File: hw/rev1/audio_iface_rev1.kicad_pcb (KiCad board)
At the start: 2 copper layers, 122 parts, among them J101 CONN_2, J102 CONN_2, J103 CONN_2, J104 CONN_2, J105 CONN_2, J501 CONN_6, J601 CONN_2, Q201 BC550, Q202 BC550, U101 USBMICROCONN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

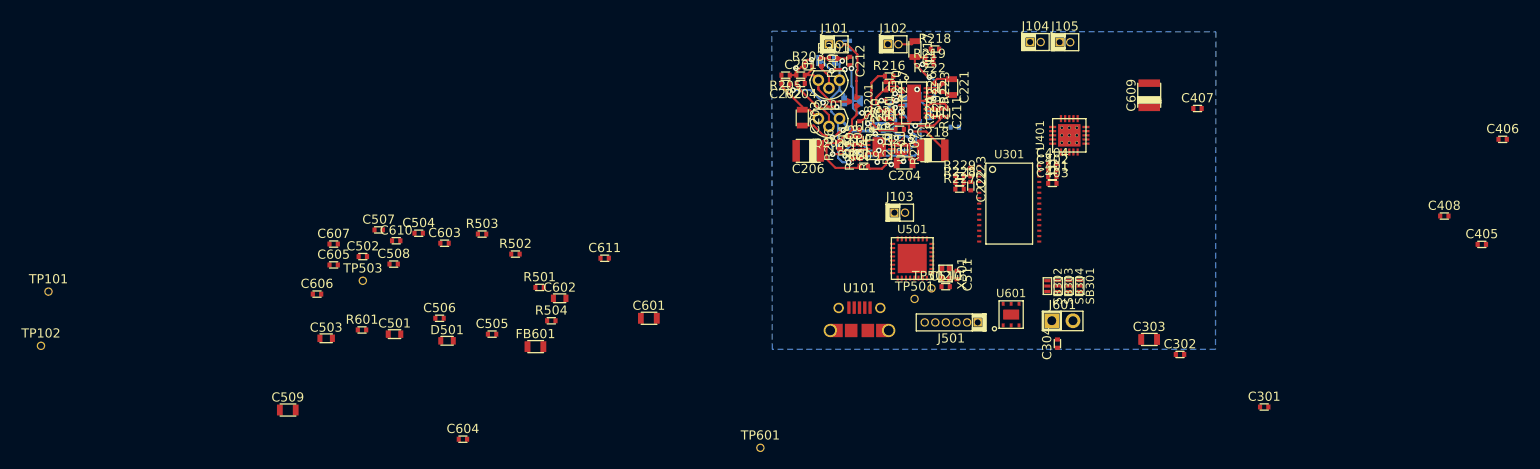
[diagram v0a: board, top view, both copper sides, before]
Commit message: Completed PCB with new K20x72 instead.
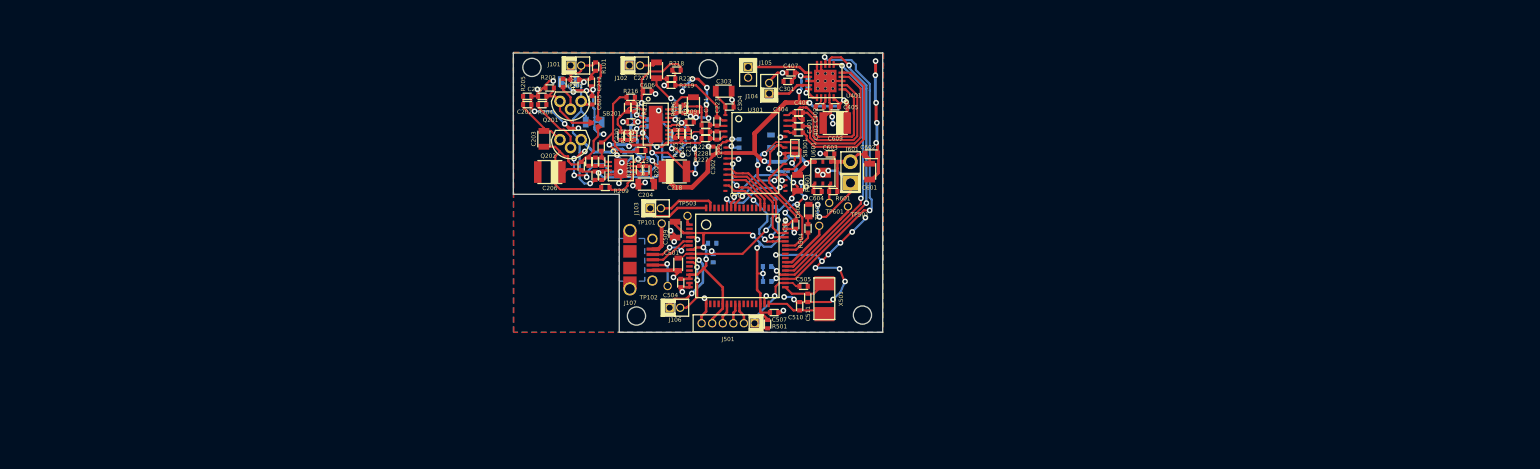
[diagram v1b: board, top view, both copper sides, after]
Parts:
- removed SB302, SB303, SB304: SB_2-1, SB_2-1
- added G***: LOGO, LOGO, F.Cu at (161.8, 112.7)
- added J106: CONN_2, HDR_2X1_50MIL, F.Cu at (140.6, 117.8)
- added SCREW_HOLE_2-56: VAL**, SCREW_HOLE_2-56, F.Cu at (163.1, 118.7)
- added SCREW_HOLE_2-56: VAL**, SCREW_HOLE_2-56, F.Cu at (144.6, 89.1)
- added SCREW_HOLE_2-56: VAL**, SCREW_HOLE_2-56, F.Cu at (123.5, 89.0)
- added SCREW_HOLE_2-56: VAL**, SCREW_HOLE_2-56, F.Cu at (136.0, 118.8)
- added VAL: OSHW, OSHW, B.Cu at (161.2, 113.3)
- C209, R101: moved to F.Cu
- C301: value 10u -> 1u
- C408, C502, C503, C508, C607, C610, C611, R502, R503: moved to B.Cu
- TP501: value TP_PTA1 -> TP_PTB3
- TP502: value TP_PTA4 -> TP_PTB16
- TP503: value TP_PTD5 -> TP_PTE0
- U501: value MK20DX128VFM5 -> K20X7_QFP64; footprint FREESCALE_QFN32 -> FREESCALE_QFP64
- X501: footprint XRCGB_F_N -> TXC_7A
- moved C406 82.0 mm to (158.0, 93.7), turned to 180 degrees
- moved C405 79.3 mm to (159.8, 93.7)
- moved C408 78.0 mm to (156.6, 90.8), turned to 270 degrees
- moved TP102 75.5 mm to (139.8, 115.2)
- moved TP101 74.0 mm to (139.0, 107.7)
- moved C301 69.2 mm to (154.2, 90.7)
- moved C302 61.1 mm to (145.2, 99.0), turned to 270 degrees
- moved C303 59.1 mm to (146.5, 91.8), turned to 180 degrees
- moved R601 58.9 mm to (159.6, 103.9), turned to 180 degrees
- moved C503 58.3 mm to (152.1, 97.8), turned to 270 degrees
- moved C604 51.9 mm to (157.7, 103.9), turned to 180 degrees
- moved C509 51.2 mm to (140.6, 108.4), turned to 90 degrees
- moved C607 50.1 mm to (148.3, 98.1), turned to 270 degrees
- moved C407 49.0 mm to (154.5, 89.6)
- moved C304 48.5 mm to (147.2, 93.7), turned to 180 degrees
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- renumbered U101 to J107
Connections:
- C301 pad 1: AGND_OUT -> AGND_IN
- C302 pad 1: AGND_OUT -> AGND_IN
- C303 pad 1: AGND_OUT -> AGND_IN
- C304 pad 1: AGND_OUT -> AGND_IN
- C401 pad 2: N-0000070 -> N-0000071
- C402 pad 2: N-0000066 -> N-0000070
- C403 pad 2: N-0000069 -> N-0000066
- C404 pad 2: N-0000068 (its old number) -> N-0000069
- C405 pad 1: AGND_OUT -> AGND_IN
- C407 pad 1: AGND_OUT -> AGND_IN
- C510 pad 1: N-0000084 -> N-00000103
- C511 pad 1: N-0000083 -> N-00000104
- J104 pad 2: AGND_OUT -> AGND_IN
- J105 pad 2: AGND_OUT -> AGND_IN
- J501 pad 1: /Microcontroller/SWCLK -> /Microcontroller/RESET
- J501 pad 3: /Microcontroller/RESET -> /Microcontroller/SWO
- J501 pad 4: /Microcontroller/SWO -> /Microcontroller/SWCLK
- R101 pad 2: +5V -> +5VA
- R218 pad 2: +5V -> +5VA
- R504 pad 2: N-0000074 -> N-0000091
- SB301 pad 1: N-0000060 -> N-0000063
- TP501 pad 1: N-0000075 -> N-0000090
- TP502 pad 1: N-0000072 (its old number) -> N-0000092
- TP503 pad 1: N-0000076 -> N-0000089
- U301 pad 17: N-0000060 -> /Microcontroller/SPI1_SOUT
- U301 pad 18: N-0000057 -> /Microcontroller/SPI1_SCK
- U301 pad 19: N-0000058 (its old number) -> /Microcontroller/SPI1_CS_CODEC
- U301 pad 22: +3V -> AGND_IN
- U301 pad 23: +3V -> AGND_IN
- U301 pad 7: AGND_OUT -> AGND_IN
- U301 pad 9: +5V -> AGND_IN
- U401 pad 1: N-0000069 -> N-0000070
- U401 pad 10: AGND_OUT -> AGND_IN
- U401 pad 13: AGND_OUT -> AGND_IN
- U401 pad 19: AGND_OUT -> AGND_IN
- U401 pad 2: N-0000070 -> N-0000069
- U401 pad 3: AGND_OUT -> AGND_IN
- U401 pad 4: N-0000068 (its old number) -> N-0000071
- U401 pad 9: AGND_OUT -> AGND_IN
- U401 pad PAD: AGND_OUT -> AGND_IN
- U501 pad 1: +3V -> N-0000089
- U501 pad 10: (no net) -> /Microcontroller/PGA0_D-
- U501 pad 11: +3V -> (no net)
- U501 pad 12: /Microcontroller/SWCLK -> (no net)
- U501 pad 13: N-0000075 -> +3V
- U501 pad 14: /Microcontroller/SWO -> +3V
- U501 pad 15: /Microcontroller/SWDIO -> AGND_IN
- U501 pad 16: N-0000072 (its old number) -> AGND_IN
- U501 pad 17: N-0000084 -> AGND_IN
- U501 pad 18: N-0000083 -> (no net)
- U501 pad 19: /Microcontroller/RESET -> (no net)
- U501 pad 2: AGND_IN -> (no net)
- U501 pad 20: /Microcontroller/I2C0_SCL -> (no net)
- U501 pad 21: /Microcontroller/I2C0_SDA -> +3V
- U501 pad 22: /Microcontroller/CODEC_SDO -> /Microcontroller/SWCLK
- U501 pad 23: /Microcontroller/CODEC_LRCK -> (no net)
- U501 pad 24: /CODEC/BICK -> /Microcontroller/SWO
- U501 pad 25: /Microcontroller/HP_~SD -> /Microcontroller/SWDIO
- U501 pad 26: /Microcontroller/CODEC_SDIN -> (no net)
- U501 pad 27: /Microcontroller/CODEC_MCLK -> (no net)
- U501 pad 28: N-0000074 -> (no net)
- U501 pad 29: /Microcontroller/CODEC_PDN -> (no net)
- U501 pad 3: /Microcontroller/USB_D+ -> +3V
- U501 pad 30: N-0000076 -> +3V
- U501 pad 31: /Microcontroller/UART0_RX -> AGND_IN
- U501 pad 32: /Microcontroller/UART0_TX -> N-00000103
- U501 pad 4: /Microcontroller/USB_D- -> AGND_IN
- U501 pad 5: +3V -> /Microcontroller/USB_D+
- U501 pad 6: +5V -> /Microcontroller/USB_D-
- U501 pad 8: AGND_IN -> +5V
- U501 pad 9: (no net) -> /Microcontroller/PGA0_D+
- X501 pad 1: N-0000083 -> N-00000104
- X501 pad 2: N-0000084 -> N-00000103
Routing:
- net AGND_IN: track 75.7 -> 209.8 mm, vias 25 -> 85
- net +5VA: track 41.2 -> 114.3 mm, vias 5 -> 13
- net +3V: track 0.00 -> 68.5 mm, vias 0 -> 8
- net /Microcontroller/I2C0_SCL: track 0.00 -> 38.8 mm, vias 0 -> 3
- net /Microcontroller/I2C0_SDA: track 0.00 -> 36.2 mm, vias 0 -> 3
- net /Microcontroller/HP_~SD: track 0.00 -> 31.2 mm, vias 0 -> 2
- net +5V: track 0.00 -> 29.6 mm, vias 0 -> 5
- net N-0000066: track 0.00 -> 18.3 mm
- net N-0000071: track 0.00 -> 17.8 mm
- net N-0000070: track 0.00 -> 17.7 mm
- net N-0000069: track 0.00 -> 16.7 mm
- net /Microcontroller/CODEC_LRCK: track 0.00 -> 14.1 mm, vias 0 -> 2
- net /Microcontroller/CODEC_PDN: track 0.00 -> 13.9 mm
- net /Microcontroller/CODEC_SDO: track 0.00 -> 12.8 mm, vias 0 -> 2
- net /CODEC/BICK: track 0.00 -> 11.9 mm
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- added copper zone on B.Cu, net (none)
- added copper zone on F.Cu, net AGND_IN
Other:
- board outline added: 44.3 x 33.5 mm
- board text added: "BRN"
- board text added: "EXT"
- board text added: "MIC"
- board text added: "R"
- board text added: "T"
- board text added: "r1a"

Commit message: Added supply voltage ADC input to monitor battery levels
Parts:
- added C512: 1u, SMD0402, B.Cu at (162.1, 105.8)
- added R505: 330k, SMD0402, B.Cu at (160.4, 105.8)
- added R506: 100k, SMD0402, B.Cu at (161.3, 105.8)
- moved TP501 4.29 mm to (157.8, 108.0)
- moved TP502 1.52 mm to (159.0, 106.9)
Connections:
- TP501 pad 1: N-0000090 -> N-0000089
- U501 pad 38: N-0000090 -> N-00000101
- U501 pad 40: (no net) -> N-0000089
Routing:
- net N-00000101: track 0.00 -> 11.4 mm, vias 0 -> 1
- net N-0000090: track 10.9 -> 0.00 mm
- net N-0000089: track 0.00 -> 5.83 mm
- net AGND_IN: track 209.8 -> 204.2 mm, vias 85 -> 83
- net VCC: track 10.8 -> 12.4 mm, vias 0 -> 1
- net (no net): track 0.00 -> 1.56 mm, vias 0 -> 2
- net N-0000080: track 6.52 -> 8.08 mm

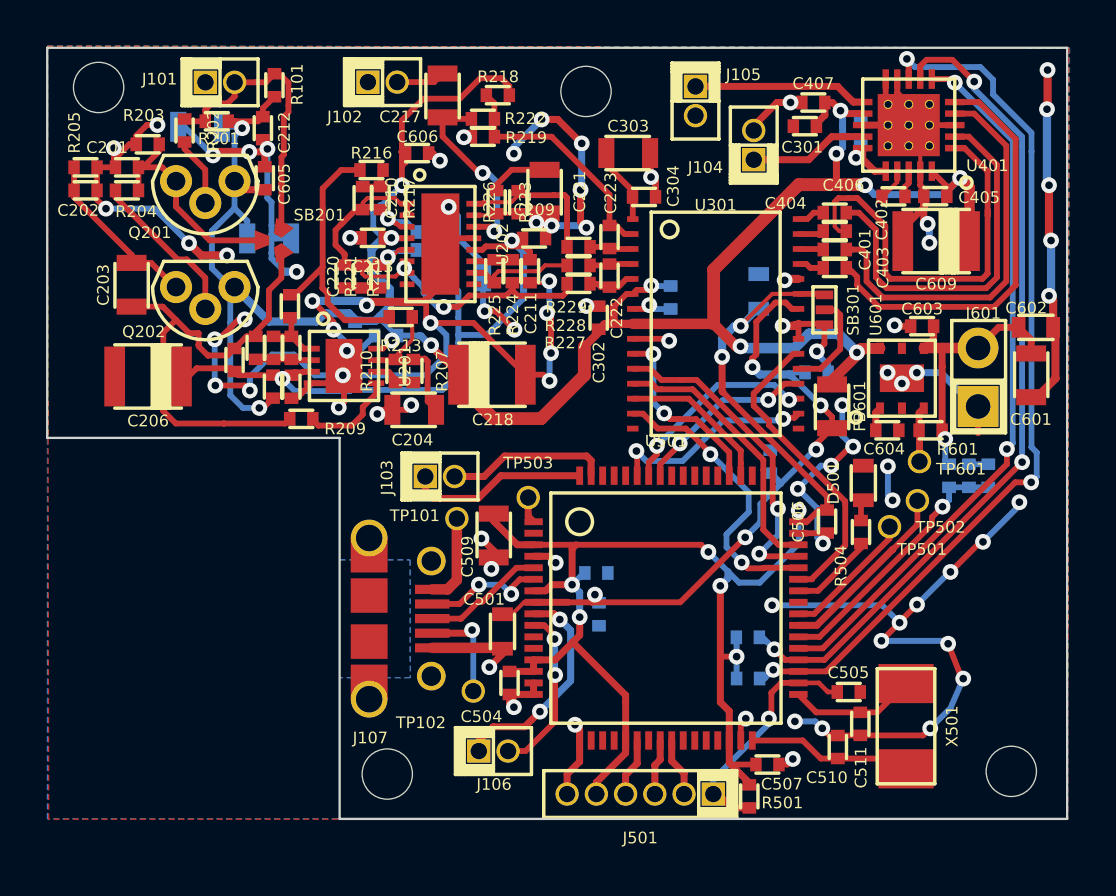
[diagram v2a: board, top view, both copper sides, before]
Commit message: Rev1a submitted -- Moved silkscreens around
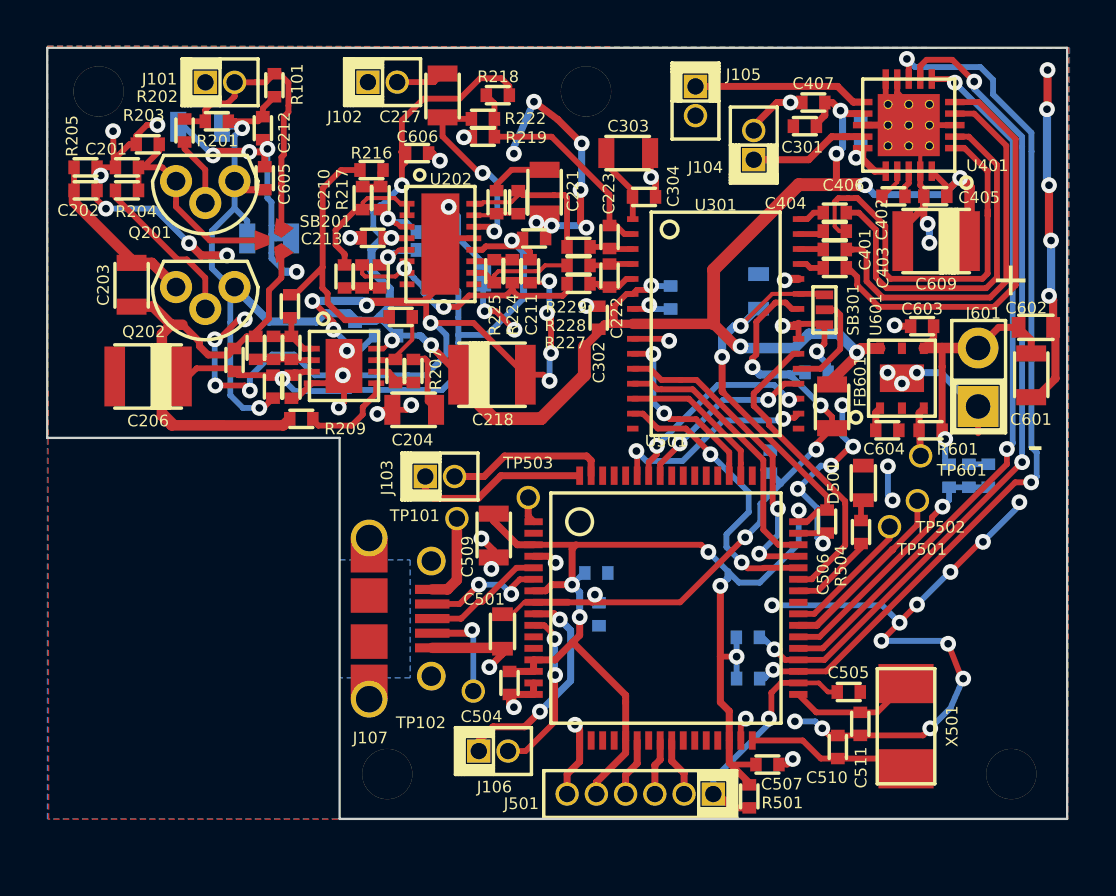
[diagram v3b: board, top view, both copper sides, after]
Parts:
- moved TP601 0.25 mm to (159.2, 105.0)
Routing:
- net N-0000052: track 21.1 -> 27.6 mm
- net AGND_IN: track 204.2 -> 206.7 mm, vias 83 -> 84
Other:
- board text added: "+"
- board text added: "-"
- board text added: "L+"
- board text added: "R+"
